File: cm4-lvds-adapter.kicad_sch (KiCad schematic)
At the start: 62 parts, among them J1 Plug_Molex_SlimStack_2x15_538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, J2 JST_SM_1x10_SM10B-SURS-TF-LF-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, J3 FFC_Amphenol_1x40_62684-40110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, U2 NTS0104_DHVQFN, U3 SN65DSI84

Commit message: [#55272] Route power
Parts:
- added TP17: TP_0.75mm_SMD, antmicro-footprints:TP_SMD_0.75mm, symbol antmicroTestPoints:TP_0.75mm_SMD
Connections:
- net GND: now also TP17.1
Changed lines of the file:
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@@
     (stroke (width 0) (type default))
   )
+  (wire (pts (xy 299.085 234.95) (xy 299.085 233.045))
+    (stroke (width 0) (type default))
+  )
   (wire (pts (xy 354.33 41.91) (xy 382.27 41.91))
     (stroke (width 0) (type default))
@@
     )
   )
+  (symbol (lib_id "antmicroTestPoints:TP_0.75mm_SMD") (at 299.085 233.045 90) (unit 1)
+    (in_bom yes) (on_board yes) (dnp no)
+    (property "Reference" "TP17" (at 299.085 226.695 0)
+      (effects (font (size 1.27 1.27) (thickness 0.15)))
+    )
+    (property "Value" "TP_0.75mm_SMD" (at 302.895 222.25 0)
+      (effects (font (size 1.27 1.27) (thickness 0.15)) (justify left bottom) hide)
+    )
+    (property "Footprint" "antmicro-footprints:TP_SMD_0.75mm" (at 305.435 222.25 0)
+      (effects (font (size 1.27 1.27) (thickness 0.15)) (justify left bottom) hide)
+    )
+    (property "Datasheet" "" (at 311.785 215.265 0)
+      (effects (font (size 1.27 1.27) (thickness 0.15)) (justify left bottom) hide)
+    )
+    (property "MPN" "" (at 310.515 222.25 0)
+      (effects (font (size 1.27 1.27) (thickness 0.15)) (justify left bottom) hide)
+    )
+    (property "Manufacturer" "" (at 305.435 222.25 0)
+      (effects (font (size 1.27 1.27) (thickness 0.15)) (justify left bottom) hide)
+    )
+    (property "Author" "Antmicro" (at 307.975 222.25 0)
+      (effects (font (size 1.27 1.27) (thickness 0.15)) (justify left bottom) hide)
+    )
+    (property "License" "Apache-2.0" (at 310.515 222.25 0)
+      (effects (font (size 1.27 1.27) (thickness 0.15)) (justify left bottom) hide)
+    )
+    (pin "1")
+    (instances
+      (project "cm4-lvds-adapter"
+        (path "/60b842dc-0853-4a25-99ac-5784ddf94d0d"
+          (reference "TP17") (unit 1)
+        )
+      )
+    )
+  )
   (symbol (lib_id "antmicropower:+9V6") (at 378.46 168.91 0) (unit 1)
     (in_bom yes) (on_board yes) (dnp no)
@@
         )
       )
+    )
+  )
+  (symbol (lib_id "antmicropower:GND") (at 299.085 234.95 0) (mirror y) (unit 1)
+    (in_bom yes) (on_board yes) (dnp no)
+    (property "Reference" "#PWR0128" (at 290.195 237.49 0)
+      (effects (font (size 1.27 1.27) (thickness 0.15)) (justify left bottom) hide)
+    )
+    (property "Value" "GND" (at 299.085 238.76 0)
+      (effects (font (size 1.27 1.27) (thickness 0.15)))
+    )
+    (property "Footprint" "" (at 290.195 242.57 0)
+      (effects (font (size 1.27 1.27) (thickness 0.15)) (justify left bottom) hide)
+    )
+    (property "Datasheet" "" (at 290.195 247.65 0)
+      (effects (font (size 1.27 1.27) (thickness 0.15)) (justify left bottom) hide)
+    )
+    (property "Author" "Antmicro" (at 290.195 242.57 0)
+      (effects (font (size 1.27 1.27) (thickness 0.15)) (justify left bottom) hide)
+    )
+    (property "License" "Apache-2.0" (at 290.195 245.11 0)
+      (effects (font (size 1.27 1.27) (thickness 0.15)) (justify left bottom) hide)
+    )
+    (pin "1")
+    (instances
+      (project "cm4-lvds-adapter"
+        (path "/60b842dc-0853-4a25-99ac-5784ddf94d0d"
+          (reference "#PWR0128") (unit 1)
+        )
+      )

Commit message: [#56078] Update symbols/footprints from lib
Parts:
- added MP1: MP_Pad6mm_Drill3mm, antmicro-footprints:MP_Pad6mm_Drill3mm, symbol antmicroMechanicalParts:MP_Pad6mm_Drill3mm
- D1, D2: value LED_G -> LED_G_0603_598-8D80-107F; footprint antmicro-footprints:LED_0603_1608Metric_R -> antmicro-footprints:LED_0603_1608Metric_G; symbol antmicroLEDIndicationDiscrete:LED_R_0603_598-8D80-107F -> antmicroLEDIndicationDiscrete:LED_G_0603_598-8D80-107F; Color (none) -> Green
- N1: footprint antmicro-footprints:antmicro-logo_scaled_12mm -> antmicro-footprints:antmicro-logo
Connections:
- net GND: now also MP1.1
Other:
- moved on the sheet: C14

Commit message: [#56708] Generate local library
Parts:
- C1, C6: footprint antmicro-footprints:C_0402_1005Metric -> cm4-lvds-adapter-footprints:C_0402_1005Metric; symbol antmicroCapacitors0402:C_10u_0402 -> cm4-lvds-adapter:C_10u_0402
- C10, C4, C42, C43, C44, C45, C46, C47, C48, C49, C5, C8, C9: footprint antmicro-footprints:C_0402_1005Metric -> cm4-lvds-adapter-footprints:C_0402_1005Metric; symbol antmicroCapacitors0402:C_100n_0402 -> cm4-lvds-adapter:C_100n_0402
- C11, C12, C13: footprint antmicro-footprints:C_0402_1005Metric -> cm4-lvds-adapter-footprints:C_0402_1005Metric; symbol antmicroCapacitors0402:C_10n_0402 -> cm4-lvds-adapter:C_10n_0402
- C14, C7: footprint antmicro-footprints:C_0402_1005Metric -> cm4-lvds-adapter-footprints:C_0402_1005Metric; symbol antmicroCapacitors0402:C_1u_0402 -> cm4-lvds-adapter:C_1u_0402
- D1, D2: footprint antmicro-footprints:LED_0603_1608Metric_G -> cm4-lvds-adapter-footprints:LED_0603_1608Metric_G; symbol antmicroLEDIndicationDiscrete:LED_G_0603_598-8D80-107F -> cm4-lvds-adapter:LED_G_0603_598-8D80-107F
- D3, D4: footprint antmicro-footprints:Nexperia_DFN-10_2.5x1mm_P0.5mm -> cm4-lvds-adapter-footprints:Nexperia_DFN-10_2.5x1mm_P0.5mm; symbol antmicroTVSDiodes:PUSB3F96X_PASS -> cm4-lvds-adapter:PUSB3F96X_PASS
- FB1: footprint antmicro-footprints:FB_0603_1608Metric -> cm4-lvds-adapter-footprints:FB_0603_1608Metric; symbol antmicroFerriteBeadsandChips:FB_220Z_2.2A_TDK-MPZ_0603 -> cm4-lvds-adapter:FB_220Z_2.2A_TDK-MPZ_0603
- J1: footprint antmicro-footprints:Conn_Plug_Molex_SlimStack_2x20_556500488 -> cm4-lvds-adapter-footprints:Conn_Plug_Molex_SlimStack_2x20_556500488; symbol antmicroB2BConnectors:Plug_Molex_SlimStack_2x20_556500488 -> cm4-lvds-adapter:Plug_Molex_SlimStack_2x20_556500488
- J2: footprint antmicro-footprints:Conn_JST_SUR_1x10_SM10B-SURS-TF-LF-SN -> cm4-lvds-adapter-footprints:Conn_JST_SUR_1x10_SM10B-SURS-TF-LF-SN; symbol antmicroWire2BoardConnectors:JST_SUR_1x10_SM10B-SURS-TF-LF-SN -> cm4-lvds-adapter:JST_SUR_1x10_SM10B-SURS-TF-LF-SN
- J3: footprint antmicro-footprints:Conn_FFC_Amphenol_1x40_62684-401100AHLF -> cm4-lvds-adapter-footprints:Conn_FFC_Amphenol_1x40_62684-401100AHLF; symbol antmicroFCCConnectors:FFC_Amphenol_1x40_62684-401100AHLF -> cm4-lvds-adapter:FFC_Amphenol_1x40_62684-401100AHLF
- MP1: footprint antmicro-footprints:MP_Pad6mm_Drill3mm -> cm4-lvds-adapter-footprints:MP_Pad6mm_Drill3mm; symbol antmicroMechanicalParts:MP_Pad6mm_Drill3mm -> cm4-lvds-adapter:MP_Pad6mm_Drill3mm
- N1: footprint antmicro-footprints:antmicro-logo -> cm4-lvds-adapter-footprints:antmicro-logo; symbol antmicroMechanicalParts:antmicro_logo -> cm4-lvds-adapter:antmicro_logo
- N2: footprint antmicro-footprints:oshw-logo -> cm4-lvds-adapter-footprints:oshw-logo; symbol antmicroMechanicalParts:oshw_logo -> cm4-lvds-adapter:oshw_logo
- R1: footprint antmicro-footprints:R_0402_1005Metric -> cm4-lvds-adapter-footprints:R_0402_1005Metric; symbol antmicroResistors0402:R_1k_0402 -> cm4-lvds-adapter:R_1k_0402
- R2: footprint antmicro-footprints:R_0402_1005Metric -> cm4-lvds-adapter-footprints:R_0402_1005Metric; symbol antmicroResistors0402:R_200R_0402 -> cm4-lvds-adapter:R_200R_0402
- R39, R40, R42, R45, R6, R7, R8: footprint antmicro-footprints:R_0402_1005Metric -> cm4-lvds-adapter-footprints:R_0402_1005Metric; symbol antmicroResistors0402:R_10k_0402 -> cm4-lvds-adapter:R_10k_0402
- R4, R47, R48, R5: footprint antmicro-footprints:R_0402_1005Metric -> cm4-lvds-adapter-footprints:R_0402_1005Metric; symbol antmicroResistors0402:R_4k7_0402 -> cm4-lvds-adapter:R_4k7_0402
- R41, R43, R46: footprint antmicro-footprints:R_0402_1005Metric -> cm4-lvds-adapter-footprints:R_0402_1005Metric; symbol antmicroResistors0402:R_0R_0402 -> cm4-lvds-adapter:R_0R_0402
- R44: footprint antmicro-footprints:R_0402_1005Metric -> cm4-lvds-adapter-footprints:R_0402_1005Metric; symbol antmicroResistors0402:R_100k_0402 -> cm4-lvds-adapter:R_100k_0402
- TP1, TP3: footprint antmicro-footprints:TP_SMD_1mm -> cm4-lvds-adapter-footprints:TP_SMD_1mm; symbol antmicroTestPoints:TP_1mm_SMD -> cm4-lvds-adapter:TP_1mm_SMD
- TP12, TP13, TP14, TP15, TP17, TP2, TP4, TP5, TP6, TP7, TP8, TP9: footprint antmicro-footprints:TP_SMD_0.75mm -> cm4-lvds-adapter-footprints:TP_SMD_0.75mm; symbol antmicroTestPoints:TP_0.75mm_SMD -> cm4-lvds-adapter:TP_0.75mm_SMD
- U2: footprint antmicro-footprints:DHVQFN-14-1EP_2.5x3mm -> cm4-lvds-adapter-footprints:DHVQFN-14-1EP_2.5x3mm; symbol antmicroLogicTranslatorsLevelShifters:NTS0104_DHVQFN -> cm4-lvds-adapter:NTS0104_DHVQFN
- U3: footprint antmicro-footprints:HTQFP-64_10x10mm_P0.5mm -> cm4-lvds-adapter-footprints:HTQFP-64_10x10mm_P0.5mm; symbol antmicroInterfaceControllers:SN65DSI84 -> cm4-lvds-adapter:SN65DSI84

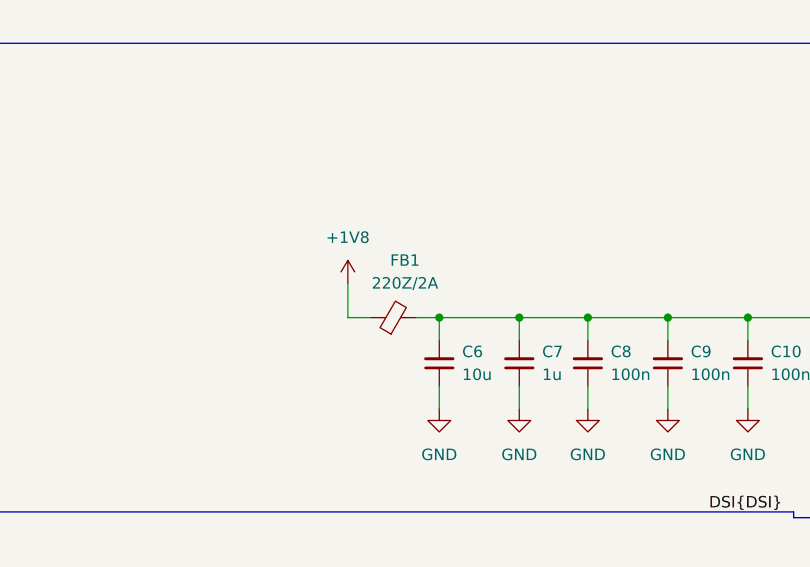
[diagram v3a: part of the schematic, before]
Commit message: [#56708] Update symbol/footprint props; Fix J1 label
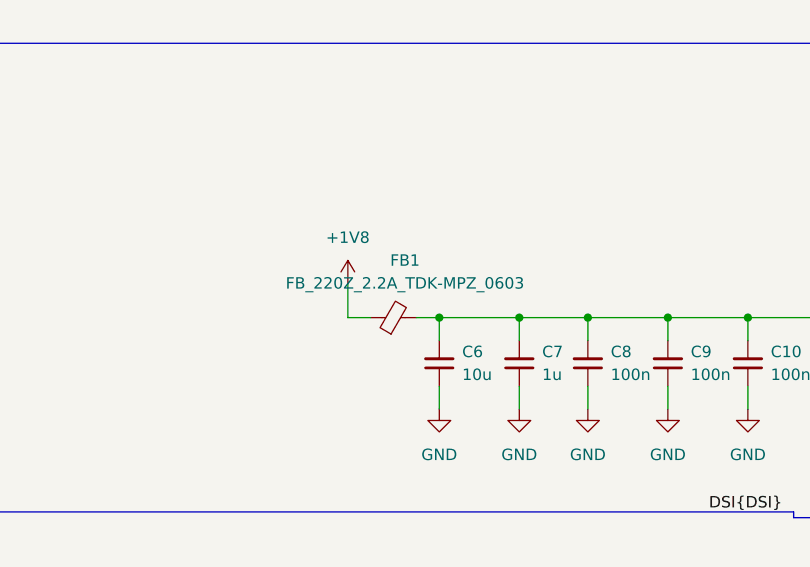
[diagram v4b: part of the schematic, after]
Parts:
- FB1: value 220Z/2A -> FB_220Z_2.2A_TDK-MPZ_0603
- J1: value Plug_Molex_SlimStack_2x15_538850308 -> Plug_Molex_SlimStack_2x20_556500488
- J2: value JST_SM_1x10_SM10B-SURS-TF-LF-SN -> JST_SUR_1x10_SM10B-SURS-TF-LF-SN
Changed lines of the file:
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@@
     (comment 1 "www.antmicro.com")
   )
+  (bus_alias "DSI" (members "D0_P" "D0_N" "D1_P" "D1_N" "D2_P" "D2_N" "D3_P" "D3_N" "CLK_P" "CLK_N"))
+  (bus_alias "DSICtrl" (members "SCL" "SDA" "~{IRQ2}" "GPIO" "~{RST}" "IRQ1" "EN" "DIM"))
+  (bus_alias "LVDS" (members "D0_P" "D0_N" "D1_P" "D1_N" "D2_P" "D2_N" "D3_P" "D3_N" "CLK_P" "CLK_N"))
   (junction (at 158.75 106.68) (diameter 0) (color 0 0 0 0)
   )
@@
     (stroke (width 0) (type default))
   )
-  (bus_alias "DSI" (members "D0_P" "D0_N" "D1_P" "D1_N" "D2_P" "D2_N" "D3_P" "D3_N" "CLK_P" "CLK_N"))
-  (bus_alias "DSICtrl" (members "SCL" "SDA" "~{IRQ2}" "GPIO" "~{RST}" "IRQ1" "EN" "DIM"))
-  (bus_alias "LVDS" (members "D0_P" "D0_N" "D1_P" "D1_N" "D2_P" "D2_N" "D3_P" "D3_N" "CLK_P" "CLK_N"))
   (bus (pts (xy 358.14 135.89) (xy 358.14 138.43))
     (stroke (width 0) (type default))
@@
       (effects (font (size 1.27 1.27)))
     )
-    (property "Value" "220Z/2A" (at 154.94 102.87 0)
+    (property "Value" "FB_220Z_2.2A_TDK-MPZ_0603" (at 154.94 102.87 0)
       (effects (font (size 1.27 1.27) (thickness 0.15)))
     )
@@
       (effects (font (size 1.27 1.27) (thickness 0.15)))
     )
-    (property "Value" "Plug_Molex_SlimStack_2x15_538850308" (at 60.96 73.66 0)
+    (property "Value" "Plug_Molex_SlimStack_2x20_556500488" (at 60.96 73.66 0)
       (effects (font (size 1.27 1.27) (thickness 0.15)) (justify left bottom) hide)
     )
@@
       (effects (font (size 1.27 1.27) (thickness 0.15)))
     )
-    (property "Value" "JST_SM_1x10_SM10B-SURS-TF-LF-SN" (at 402.59 44.45 0)
+    (property "Value" "JST_SUR_1x10_SM10B-SURS-TF-LF-SN" (at 402.59 44.45 0)
       (effects (font (size 1.27 1.27) (thickness 0.15)) (justify left bottom) hide)
     )
@@
     (instances
       (project "cm4-lvds-adapter"
-        (path "/60b842dc-0853-4a25-99ac-5784ddf94d0d" (page "3"))
+        (path "/60b842dc-0853-4a25-99ac-5784ddf94d0d" (page "2"))
       )
     )

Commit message: [#57456] Remove loclib
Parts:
- C1, C6: footprint cm4-lvds-adapter-footprints:C_0402_1005Metric -> antmicro-footprints:C_0402_1005Metric; symbol cm4-lvds-adapter:C_10u_0402 -> antmicroCapacitors0402:C_10u_0402
- C10, C4, C42, C43, C44, C45, C46, C47, C48, C49, C5, C8, C9: footprint cm4-lvds-adapter-footprints:C_0402_1005Metric -> antmicro-footprints:C_0402_1005Metric; symbol cm4-lvds-adapter:C_100n_0402 -> antmicroCapacitors0402:C_100n_0402
- C11, C12, C13: footprint cm4-lvds-adapter-footprints:C_0402_1005Metric -> antmicro-footprints:C_0402_1005Metric; symbol cm4-lvds-adapter:C_10n_0402 -> antmicroCapacitors0402:C_10n_0402
- C14, C7: footprint cm4-lvds-adapter-footprints:C_0402_1005Metric -> antmicro-footprints:C_0402_1005Metric; symbol cm4-lvds-adapter:C_1u_0402 -> antmicroCapacitors0402:C_1u_0402
- D1, D2: footprint cm4-lvds-adapter-footprints:LED_0603_1608Metric_G -> antmicro-footprints:LED_0603_1608Metric_G; symbol cm4-lvds-adapter:LED_G_0603_598-8D80-107F -> antmicroLEDIndicationDiscrete:LED_G_0603_598-8D80-107F
- D3, D4: footprint cm4-lvds-adapter-footprints:Nexperia_DFN-10_2.5x1mm_P0.5mm -> antmicro-footprints:Nexperia_DFN-10_2.5x1mm_P0.5mm; symbol cm4-lvds-adapter:PUSB3F96X_PASS -> antmicroTVSDiodes:PUSB3F96X_PASS
- FB1: footprint cm4-lvds-adapter-footprints:FB_0603_1608Metric -> antmicro-footprints:FB_0603_1608Metric; symbol cm4-lvds-adapter:FB_220Z_2.2A_TDK-MPZ_0603 -> antmicroFerriteBeadsandChips:FB_220Z_2.2A_TDK-MPZ_0603
- J1: footprint cm4-lvds-adapter-footprints:Conn_Plug_Molex_SlimStack_2x20_556500488 -> antmicro-footprints:Conn_Plug_Molex_SlimStack_2x20_556500488; symbol cm4-lvds-adapter:Plug_Molex_SlimStack_2x20_556500488 -> antmicroB2BConnectors:Plug_Molex_SlimStack_2x20_556500488
- J2: footprint cm4-lvds-adapter-footprints:Conn_JST_SUR_1x10_SM10B-SURS-TF-LF-SN -> antmicro-footprints:Conn_JST_SUR_1x10_SM10B-SURS-TF-LF-SN; symbol cm4-lvds-adapter:JST_SUR_1x10_SM10B-SURS-TF-LF-SN -> antmicroWire2BoardConnectors:JST_SUR_1x10_SM10B-SURS-TF-LF-SN
- J3: footprint cm4-lvds-adapter-footprints:Conn_FFC_Amphenol_1x40_62684-401100AHLF -> antmicro-footprints:Conn_FFC_Amphenol_1x40_62684-401100AHLF; symbol cm4-lvds-adapter:FFC_Amphenol_1x40_62684-401100AHLF -> antmicroFCCConnectors:FFC_Amphenol_1x40_62684-401100AHLF
- MP1: footprint cm4-lvds-adapter-footprints:MP_Pad6mm_Drill3mm -> antmicro-footprints:MP_Pad6mm_Drill3mm; symbol cm4-lvds-adapter:MP_Pad6mm_Drill3mm -> antmicroMechanicalParts:MP_Pad6mm_Drill3mm
- N1: footprint cm4-lvds-adapter-footprints:antmicro-logo -> antmicro-footprints:antmicro-logo; symbol cm4-lvds-adapter:antmicro_logo -> antmicroMechanicalParts:antmicro_logo
- N2: footprint cm4-lvds-adapter-footprints:oshw-logo -> antmicro-footprints:oshw-logo; symbol cm4-lvds-adapter:oshw_logo -> antmicroMechanicalParts:oshw_logo
- R1: footprint cm4-lvds-adapter-footprints:R_0402_1005Metric -> antmicro-footprints:R_0402_1005Metric; symbol cm4-lvds-adapter:R_1k_0402 -> antmicroResistors0402:R_1k_0402
- R2: footprint cm4-lvds-adapter-footprints:R_0402_1005Metric -> antmicro-footprints:R_0402_1005Metric; symbol cm4-lvds-adapter:R_200R_0402 -> antmicroResistors0402:R_200R_0402
- R39, R40, R42, R45, R6, R7, R8: footprint cm4-lvds-adapter-footprints:R_0402_1005Metric -> antmicro-footprints:R_0402_1005Metric; symbol cm4-lvds-adapter:R_10k_0402 -> antmicroResistors0402:R_10k_0402
- R4, R47, R48, R5: footprint cm4-lvds-adapter-footprints:R_0402_1005Metric -> antmicro-footprints:R_0402_1005Metric; symbol cm4-lvds-adapter:R_4k7_0402 -> antmicroResistors0402:R_4k7_0402
- R41, R43, R46: footprint cm4-lvds-adapter-footprints:R_0402_1005Metric -> antmicro-footprints:R_0402_1005Metric; symbol cm4-lvds-adapter:R_0R_0402 -> antmicroResistors0402:R_0R_0402
- R44: footprint cm4-lvds-adapter-footprints:R_0402_1005Metric -> antmicro-footprints:R_0402_1005Metric; symbol cm4-lvds-adapter:R_100k_0402 -> antmicroResistors0402:R_100k_0402
- TP1, TP3: footprint cm4-lvds-adapter-footprints:TP_SMD_1mm -> antmicro-footprints:TP_SMD_1mm; symbol cm4-lvds-adapter:TP_1mm_SMD -> antmicroTestPoints:TP_1mm_SMD
- TP12, TP13, TP14, TP15, TP17, TP2, TP4, TP5, TP6, TP7, TP8, TP9: footprint cm4-lvds-adapter-footprints:TP_SMD_0.75mm -> antmicro-footprints:TP_SMD_0.75mm; symbol cm4-lvds-adapter:TP_0.75mm_SMD -> antmicroTestPoints:TP_0.75mm_SMD
- U2: footprint cm4-lvds-adapter-footprints:DHVQFN-14-1EP_2.5x3mm -> antmicro-footprints:DHVQFN-14-1EP_2.5x3mm; symbol cm4-lvds-adapter:NTS0104_DHVQFN -> antmicroLogicTranslatorsLevelShifters:NTS0104_DHVQFN
- U3: footprint cm4-lvds-adapter-footprints:HTQFP-64_10x10mm_P0.5mm -> antmicro-footprints:HTQFP-64_10x10mm_P0.5mm; symbol cm4-lvds-adapter:SN65DSI84 -> antmicroInterfaceControllers:SN65DSI84

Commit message: [#57456] Fix 3d model links, update schematic structure
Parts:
- removed C1, C6: C_10u_0402, antmicro-footprints:C_0402_1005Metric, symbol antmicroCapacitors0402:C_10u_0402
- removed C10, C4, C42, C43, C44, C45, C46, C47, C48, C49, C5, C8, C9: C_100n_0402, antmicro-footprints:C_0402_1005Metric, symbol antmicroCapacitors0402:C_100n_0402
- removed C11, C12, C13: C_10n_0402, antmicro-footprints:C_0402_1005Metric, symbol antmicroCapacitors0402:C_10n_0402
- removed C14, C7: C_1u_0402, antmicro-footprints:C_0402_1005Metric, symbol antmicroCapacitors0402:C_1u_0402
- removed D1, D2: LED_G_0603_598-8D80-107F, antmicro-footprints:LED_0603_1608Metric_G, symbol antmicroLEDIndicationDiscrete:LED_G_0603_598-8D80-107F
- removed D3, D4: PUSB3F96X_PASS, antmicro-footprints:Nexperia_DFN-10_2.5x1mm_P0.5mm, symbol antmicroTVSDiodes:PUSB3F96X_PASS
- removed FB1: FB_220Z_2.2A_TDK-MPZ_0603, antmicro-footprints:FB_0603_1608Metric, symbol antmicroFerriteBeadsandChips:FB_220Z_2.2A_TDK-MPZ_0603
- removed J1: Plug_Molex_SlimStack_2x20_556500488, antmicro-footprints:Conn_Plug_Molex_SlimStack_2x20_556500488, symbol antmicroB2BConnectors:Plug_Molex_SlimStack_2x20_556500488
- removed J2: JST_SUR_1x10_SM10B-SURS-TF-LF-SN, antmicro-footprints:Conn_JST_SUR_1x10_SM10B-SURS-TF-LF-SN, symbol antmicroWire2BoardConnectors:JST_SUR_1x10_SM10B-SURS-TF-LF-SN
- removed J3: FFC_Amphenol_1x40_62684-401100AHLF, antmicro-footprints:Conn_FFC_Amphenol_1x40_62684-401100AHLF, symbol antmicroFCCConnectors:FFC_Amphenol_1x40_62684-401100AHLF
- removed MP1: MP_Pad6mm_Drill3mm, antmicro-footprints:MP_Pad6mm_Drill3mm, symbol antmicroMechanicalParts:MP_Pad6mm_Drill3mm
- removed R1: R_1k_0402, antmicro-footprints:R_0402_1005Metric, symbol antmicroResistors0402:R_1k_0402
- removed R2: R_200R_0402, antmicro-footprints:R_0402_1005Metric, symbol antmicroResistors0402:R_200R_0402
- removed R39, R40, R42, R45, R6, R7, R8: R_10k_0402, antmicro-footprints:R_0402_1005Metric, symbol antmicroResistors0402:R_10k_0402
- removed R4, R47, R48, R5: R_4k7_0402, antmicro-footprints:R_0402_1005Metric, symbol antmicroResistors0402:R_4k7_0402
- removed R41, R43, R46: R_0R_0402, antmicro-footprints:R_0402_1005Metric, symbol antmicroResistors0402:R_0R_0402
- removed R44: R_100k_0402, antmicro-footprints:R_0402_1005Metric, symbol antmicroResistors0402:R_100k_0402
- removed TP1, TP3: TP_1mm_SMD, antmicro-footprints:TP_SMD_1mm, symbol antmicroTestPoints:TP_1mm_SMD
- removed TP12, TP13, TP14, TP15, TP17, TP2, TP4, TP5, TP6, TP7, TP8, TP9: TP_0.75mm_SMD, antmicro-footprints:TP_SMD_0.75mm, symbol antmicroTestPoints:TP_0.75mm_SMD
- removed U2: NTS0104_DHVQFN, antmicro-footprints:DHVQFN-14-1EP_2.5x3mm, symbol antmicroLogicTranslatorsLevelShifters:NTS0104_DHVQFN
- removed U3: SN65DSI84, antmicro-footprints:HTQFP-64_10x10mm_P0.5mm, symbol antmicroInterfaceControllers:SN65DSI84
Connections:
- no-connect marks 18 -> 0
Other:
- added sheet Antmicro CM4 Baseboard DSI Connector  (dsi-connector.kicad_sch)
- added sheet DSI to LVDS (dsi-to-lvds.kicad_sch)
- added sheet LVDS and Touchscreen Connectors (lvds-connector.kicad_sch)
- note removed: "Antmicro CM4 Baseboard DSI Connector"
- note removed: "DSI -> LVDS"
- note removed: "Display MPN: CLAA080XA12LE"
- note removed: "Display configuration"
- note removed: "Display decoupling capacitors"
- note removed: "Global reset (active low)"
- note removed: "I2C touchscreen connector"
- note removed: "LVDS connector"
- note removed: "Max 45mA"
- note removed: "Note: IO's are 3V3 level"
- note removed: "Note: I_{2}C address selection: ADDR | write address 1 | 0x5A 0 | 0x58"
- note removed: "Note: SN65DSI83*-Q1 should be here drop-in compatible"
- note removed: "Set display orientation as NORMAL"
- note removed: "VDD"
- note removed: "Vcom"
- note removed: "select 8bit input"
- moved on the sheet: N1, N2
